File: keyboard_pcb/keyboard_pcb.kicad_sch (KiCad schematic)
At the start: 190 parts, among them SW1 SW_Push, U1 ATmega32U4-A, Y1 16MHz

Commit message: Complete electronic schematic
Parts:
- SW1: renamed from ESC; value MX-NoLED -> ESC
- SW10: renamed from F9; value MX-NoLED -> F9
- SW11: renamed from F10; value MX-NoLED -> F10
- SW12: renamed from F11; value MX-NoLED -> F11
- SW13: renamed from F12; value MX-NoLED -> F12
- SW14: renamed from PRNTSC; value MX-NoLED -> PRNTSC
- SW15: renamed from SCRLLK; value MX-NoLED -> SCRLLK
- SW16: renamed from PBRK; value MX-NoLED -> PBRK
- SW17: renamed from TILDE; value MX-NoLED -> `
- SW18: renamed from N1; value MX-NoLED -> #1
- SW19: renamed from N2; value MX-NoLED -> #2
- SW2: renamed from F1; value MX-NoLED -> F1
- SW20: renamed from N3; value MX-NoLED -> #3
- SW21: renamed from N4; value MX-NoLED -> #4
- SW22: renamed from N5; value MX-NoLED -> #5
- SW23: renamed from N6; value MX-NoLED -> #6
- SW24: renamed from N7; value MX-NoLED -> #7
- SW25: renamed from N8; value MX-NoLED -> #8
- SW26: renamed from N9; value MX-NoLED -> #9
- SW27: renamed from N0; value MX-NoLED -> #0
- SW28: renamed from -; value MX-NoLED -> -
- SW29: renamed from =; value MX-NoLED -> =
- SW3: renamed from F2; value MX-NoLED -> F2
- SW30: renamed from BKSPC; value MX-NoLED -> BKSPC
- SW31: renamed from INS; value MX-NoLED -> INS
- SW32: renamed from HOME; value MX-NoLED -> HOME
- SW33: renamed from PGUP; value MX-NoLED -> PGUP
- SW34: renamed from TAB; value MX-NoLED -> TAB
- SW35: renamed from Q; value MX-NoLED -> Q
- SW36: renamed from W; value MX-NoLED -> W
- SW37: renamed from E; value MX-NoLED -> E
- SW38: renamed from R; value MX-NoLED -> R
- SW39: renamed from T; value MX-NoLED -> T
- SW4: renamed from F3; value MX-NoLED -> F3
- SW40: renamed from Y; value MX-NoLED -> Y
- SW41: renamed from U; value MX-NoLED -> U
- SW42: renamed from I; value MX-NoLED -> I
- SW43: renamed from O; value MX-NoLED -> O
- SW44: renamed from P; value MX-NoLED -> P
- SW45: renamed from [; value MX-NoLED -> [
- SW46: renamed from ]; value MX-NoLED -> ]
- SW47: renamed from \; value MX-NoLED -> \
- SW48: renamed from DEL; value MX-NoLED -> DEL
- SW49: renamed from END; value MX-NoLED -> END
- SW5: renamed from F4; value MX-NoLED -> F4
- SW50: renamed from PGDN; value MX-NoLED -> PGDN
- SW51: renamed from CAPSLK; value MX-NoLED -> CAPSLK
- SW52: renamed from A; value MX-NoLED -> A
- SW53: renamed from S; value MX-NoLED -> S
- SW54: renamed from D; value MX-NoLED -> D
- SW55: renamed from F; value MX-NoLED -> F
- SW56: renamed from G; value MX-NoLED -> G
- SW57: renamed from H; value MX-NoLED -> H
- SW58: renamed from J; value MX-NoLED -> J
- SW59: renamed from K; value MX-NoLED -> K
- SW6: renamed from F5; value MX-NoLED -> F5
- SW60: renamed from L; value MX-NoLED -> L
- SW61: renamed from ;; value MX-NoLED -> ;
- SW62: renamed from '; value MX-NoLED -> '
- SW63: renamed from ENTER; value MX-NoLED -> ENTER
- SW64: renamed from LSHIFT; value MX-NoLED -> LSHIFT
- SW65: renamed from Z; value MX-NoLED -> Z
- SW66: renamed from X; value MX-NoLED -> X
- SW67: renamed from C; value MX-NoLED -> C
- SW68: renamed from V; value MX-NoLED -> V
- SW69: renamed from B; value MX-NoLED -> B
- SW7: renamed from F6; value MX-NoLED -> F6
- SW70: renamed from N; value MX-NoLED -> N
- SW71: renamed from M; value MX-NoLED -> M
- SW72: renamed from ,; value MX-NoLED -> ,
- SW73: renamed from .; value MX-NoLED -> .
- SW74: renamed from /; value MX-NoLED -> /
- SW75: renamed from RSHIFT; value MX-NoLED -> RSHIFT
- SW76: renamed from UP; value MX-NoLED -> UP
- SW77: renamed from LCTRL; value MX-NoLED -> LCTRL
- SW78: renamed from LWIN; value MX-NoLED -> LWIN
- SW79: renamed from LALT; value MX-NoLED -> LALT
- SW8: renamed from F7; value MX-NoLED -> F7
- SW80: renamed from SPACE; value MX-NoLED -> SPACE
- SW81: renamed from RALT; value MX-NoLED -> RALT
- SW82: renamed from RWIN; value MX-NoLED -> RWIN
- SW83: renamed from MENU; value MX-NoLED -> MENU
- SW84: renamed from RCTRL; value MX-NoLED -> RCTRL
- SW85: renamed from LEFT; value MX-NoLED -> LEFT
- SW86: renamed from DOWN; value MX-NoLED -> DOWN
- SW87: renamed from RIGHT; value MX-NoLED -> RIGHT
- SW9: renamed from F8; value MX-NoLED -> F8
- renumbered D86 to D1, D96 to D10, D97 to D11, D98 to D12, D99 to D13, D100 to D14, D101 to D15, D102 to D16, D1 to D17, D6 to D18, D11 to D19, D88 to D2, D16 to D20, D26 to D22, D31 to D23, D36 to D24, D41 to D25, D46 to D26, D51 to D27, D56 to D28, D61 to D29, D89 to D3, D66 to D30, D71 to D31, D76 to D32, D81 to D33, D2 to D34, D7 to D35, D12 to D36, D17 to D37, D22 to D38, D27 to D39, D90 to D4, D32 to D40, D37 to D41, D47 to D43, D52 to D44, D57 to D45, D62 to D46, D67 to D47, D72 to D48, D77 to D49, D91 to D5, D82 to D50, D3 to D51, D8 to D52, D13 to D53, D18 to D54, D23 to D55, D28 to D56, D33 to D57, D38 to D58, D43 to D59, D92 to D6, D48 to D60, D53 to D61, D58 to D62, D68 to D63, D4 to D64, D14 to D65, D19 to D66, D24 to D67, D29 to D68, D34 to D69, D93 to D7, D39 to D70, D44 to D71, D49 to D72, D54 to D73, D59 to D74, D69 to D75, D79 to D76, D5 to D77, D10 to D78, D15 to D79, D94 to D8, D35 to D80, D55 to D81, D60 to D82, D65 to D83, D70 to D84, D75 to D85, D80 to D86, D85 to D87, D95 to D9, SW1 to SW88
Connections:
- net COL0: now also U1.25 (PD4)
- net COL1: now also U1.26 (PD6)
- net COL10: now also U1.9 (PB1)
- net COL11: now also U1.10 (PB2)
- net COL12: now also U1.11 (PB3)
- net COL13: now also U1.18 (PD0)
- net COL14: now also U1.19 (PD1)
- net COL15: now also U1.20 (PD2)
- net COL16: now also U1.21 (PD3)
- net COL2: now also U1.27 (PD7)
- net COL3: now also U1.28 (PB4)
- net COL5: now also U1.29 (PB5)
- net COL6: now also U1.30 (PB6)
- net COL7: now also U1.31 (PC6)
- net COL8: now also U1.32 (PC7)
- net COL9: now also U1.8 (PB0)
- net ROW0: now also U1.36 (PF7)
- net ROW1: now also U1.37 (PF6)
- net ROW2: now also U1.38 (PF5)
- net ROW3: now also U1.39 (PF4)
- net ROW4: now also U1.40 (PF1)
- net ROW5: now also U1.41 (PF0)
- no-connect marks 0 -> 6
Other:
- moved on the sheet: F1

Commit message: PCB layout first draft
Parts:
- C1: value C_Small -> 1uF; footprint (none) -> Capacitor_SMD:C_0805_2012Metric_Pad1.18x1.45mm_HandSolder
- C2, C3, C4, C5, C6, C7: footprint (none) -> Capacitor_SMD:C_0805_2012Metric_Pad1.18x1.45mm_HandSolder
- D1, D10, D11, D12, D13, D14, D15, D16, D17, D18, D19, D2, D20, D21, D22, D23, D24, D25, D26, D27, D28, D29, D3, D30, D31, D32, D33, D34, D35, D36, D37, D38, D39, D4, D40, D41, D42, D43, D44, D45, D46, D47, D48, D49, D5, D50, D51, D52, D53, D54, D55, D56, D57, D58, D59, D6, D60, D61, D62, D63, D64, D65, D66, D67, D68, D69, D7, D70, D71, D72, D73, D74, D75, D76, D77, D78, D79, D8, D80, D81, D82, D83, D84, D85, D86, D87, D9: footprint (none) -> Diode_SMD:D_SOD-123
- F1: footprint (none) -> Fuse:Fuse_1206_3216Metric_Pad1.42x1.75mm_HandSolder
- R1, R2, R3, R4: footprint (none) -> Resistor_SMD:R_0805_2012Metric_Pad1.20x1.40mm_HandSolder
- SW1, SW10, SW11, SW12, SW13, SW14, SW15, SW16, SW17, SW18, SW19, SW2, SW20, SW21, SW22, SW23, SW24, SW25, SW26, SW27, SW28, SW29, SW3, SW31, SW32, SW33, SW35, SW36, SW37, SW38, SW39, SW4, SW40, SW41, SW42, SW43, SW44, SW45, SW46, SW48, SW49, SW5, SW50, SW52, SW53, SW54, SW55, SW56, SW57, SW58, SW59, SW6, SW60, SW61, SW62, SW65, SW66, SW67, SW68, SW69, SW7, SW70, SW71, SW72, SW73, SW74, SW76, SW8, SW85, SW86, SW87, SW9: footprint (none) -> Button_Switch_Keyboard:SW_Cherry_MX_1.00u_PCB
- SW30: footprint (none) -> Button_Switch_Keyboard:SW_Cherry_MX_2.00u_PCB
- SW34, SW47: footprint (none) -> Button_Switch_Keyboard:SW_Cherry_MX_1.50u_PCB
- SW51: footprint (none) -> Button_Switch_Keyboard:SW_Cherry_MX_1.75u_PCB
- SW63, SW64: footprint (none) -> Button_Switch_Keyboard:SW_Cherry_MX_2.25u_PCB
- SW75: footprint (none) -> Button_Switch_Keyboard:SW_Cherry_MX_2.75u_PCB
- SW77, SW78, SW79, SW81, SW82, SW83, SW84: footprint (none) -> Button_Switch_Keyboard:SW_Cherry_MX_1.25u_PCB
- SW80: footprint (none) -> Button_Switch_Keyboard:SW_Cherry_MX_6.25u_PCB
- SW88: footprint (none) -> Button_Switch_SMD:SW_SPST_SKQG_WithStem
- USB1: footprint (none) -> random-keyboard-parts:Molex-0548190589
- Y1: footprint (none) -> Crystal:Crystal_SMD_3225-4Pin_3.2x2.5mm_HandSoldering

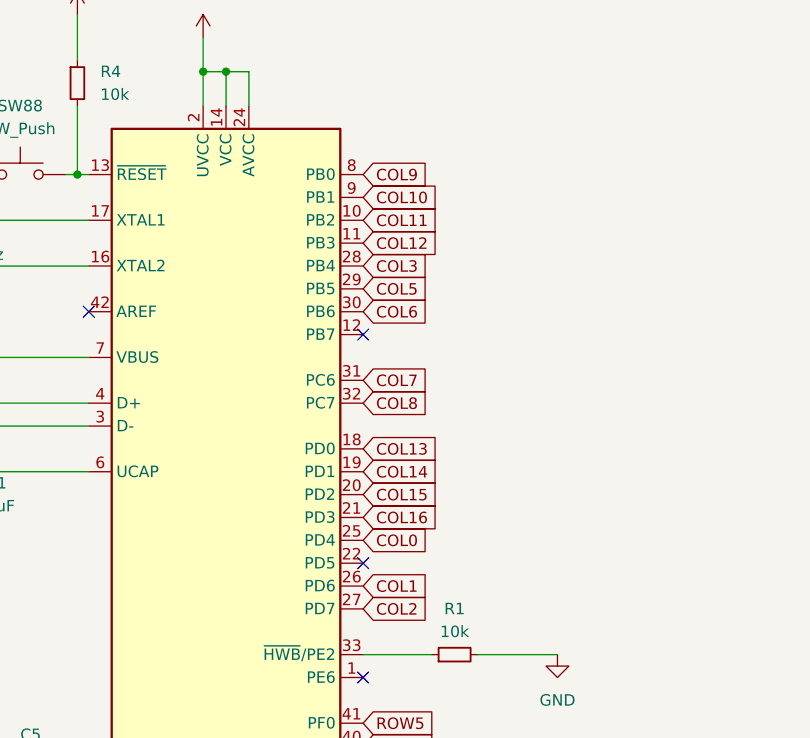
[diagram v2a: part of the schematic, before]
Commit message: Add row/column traces
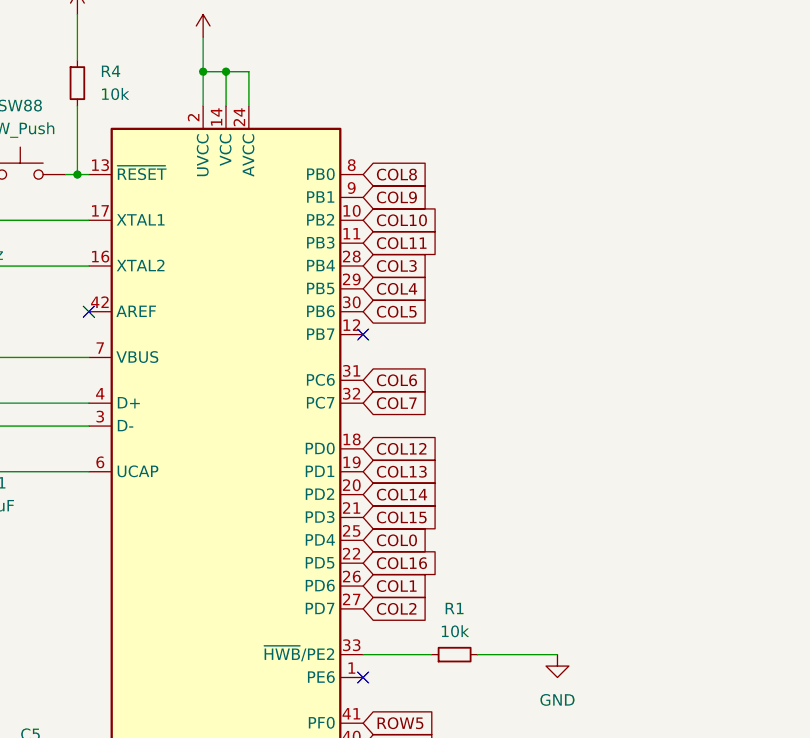
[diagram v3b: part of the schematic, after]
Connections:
- net COL10: now also U1.10 (PB2); no longer U1.9 (PB1)
- net COL11: now also U1.11 (PB3); no longer U1.10 (PB2)
- net COL12: now also U1.18 (PD0); no longer U1.11 (PB3)
- net COL13: now also U1.19 (PD1); no longer U1.18 (PD0)
- net COL14: now also U1.20 (PD2); no longer U1.19 (PD1)
- net COL15: now also U1.21 (PD3); no longer U1.20 (PD2)
- net COL16: now also U1.22 (PD5); no longer U1.21 (PD3)
- net COL4: now also U1.29 (PB5)
- net COL5: now also U1.30 (PB6); no longer U1.29 (PB5)
- net COL6: now also U1.31 (PC6); no longer U1.30 (PB6)
- net COL7: now also U1.32 (PC7); no longer U1.31 (PC6)
- net COL8: now also U1.8 (PB0); no longer U1.32 (PC7)
- net COL9: now also U1.9 (PB1); no longer U1.8 (PB0)
- no-connect marks 6 -> 5
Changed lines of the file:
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@@
 	)
 	(no_connect
-		(at 171.45 219.71)
-	)
-	(no_connect
 		(at 323.85 195.58)
 	)
@@
 	(global_label "COL14"
 		(shape input)
-		(at 171.45 209.55 0)
+		(at 171.45 212.09 0)
 		(fields_autoplaced yes)
 		(effects
@@
 		)
 		(property "Intersheetrefs" "${INTERSHEET_REFS}"
-			(at 180.4828 209.55 0)
+			(at 180.4828 212.09 0)
 			(effects
 				(font
@@
 		)
 	)
+	(global_label "COL4"
+		(shape input)
+		(at 171.45 189.23 0)
+		(fields_autoplaced yes)
+		(effects
+			(font
+				(size 1.27 1.27)
+			)
+			(justify left)
+		)
+		(property "Intersheetrefs" "${INTERSHEET_REFS}"
+			(at 179.2733 189.23 0)
+			(effects
+				(font
+					(size 1.27 1.27)
+				)
+				(justify left)
+				(hide yes)
+			)
+		)
+	)
 	(global_label "COL7"
 		(shape input)
-		(at 171.45 199.39 0)
+		(at 171.45 201.93 0)
 		(fields_autoplaced yes)
 		(effects
@@
 		)
 		(property "Intersheetrefs" "${INTERSHEET_REFS}"
-			(at 179.2733 199.39 0)
+			(at 179.2733 201.93 0)
 			(effects
 				(font
@@
 	(global_label "COL10"
 		(shape input)
-		(at 171.45 179.07 0)
+		(at 171.45 181.61 0)
 		(fields_autoplaced yes)
 		(effects
@@
 		)
 		(property "Intersheetrefs" "${INTERSHEET_REFS}"
-			(at 180.4828 179.07 0)
+			(at 180.4828 181.61 0)
 			(effects
 				(font
@@
 	(global_label "COL8"
 		(shape input)
-		(at 171.45 201.93 0)
+		(at 171.45 176.53 0)
 		(fields_autoplaced yes)
 		(effects
@@
 		)
 		(property "Intersheetrefs" "${INTERSHEET_REFS}"
-			(at 179.2733 201.93 0)
+			(at 179.2733 176.53 0)
 			(effects
 				(font
@@
 	(global_label "COL15"
 		(shape input)
-		(at 171.45 212.09 0)
+		(at 171.45 214.63 0)
 		(fields_autoplaced yes)
 		(effects
@@
 		)
 		(property "Intersheetrefs" "${INTERSHEET_REFS}"
-			(at 180.4828 212.09 0)
+			(at 180.4828 214.63 0)
 			(effects
 				(font
@@
 	(global_label "COL11"
 		(shape input)
-		(at 171.45 181.61 0)
+		(at 171.45 184.15 0)
 		(fields_autoplaced yes)
 		(effects
@@
 		)
 		(property "Intersheetrefs" "${INTERSHEET_REFS}"
-			(at 180.4828 181.61 0)
+			(at 180.4828 184.15 0)
 			(effects
 				(font
@@
 	(global_label "COL9"
 		(shape input)
-		(at 171.45 176.53 0)
+		(at 171.45 179.07 0)
 		(fields_autoplaced yes)
 		(effects
@@
 		)
 		(property "Intersheetrefs" "${INTERSHEET_REFS}"
-			(at 179.2733 176.53 0)
+			(at 179.2733 179.07 0)
 			(effects
 				(font
@@
 	(global_label "COL12"
 		(shape input)
-		(at 171.45 184.15 0)
+		(at 171.45 207.01 0)
 		(fields_autoplaced yes)
 		(effects
@@
 		)
 		(property "Intersheetrefs" "${INTERSHEET_REFS}"
-			(at 180.4828 184.15 0)
+			(at 180.4828 207.01 0)
 			(effects
 				(font
@@
 	(global_label "COL5"
 		(shape input)
-		(at 171.45 189.23 0)
+		(at 171.45 191.77 0)
 		(fields_autoplaced yes)
 		(effects
@@
 		)
 		(property "Intersheetrefs" "${INTERSHEET_REFS}"
-			(at 179.2733 189.23 0)
+			(at 179.2733 191.77 0)
 			(effects
 				(font
@@
 	(global_label "COL13"
 		(shape input)
-		(at 171.45 207.01 0)
+		(at 171.45 209.55 0)
 		(fields_autoplaced yes)
 		(effects
@@
 		)
 		(property "Intersheetrefs" "${INTERSHEET_REFS}"
-			(at 180.4828 207.01 0)
+			(at 180.4828 209.55 0)
 			(effects
 				(font
@@
 	(global_label "COL16"
 		(shape input)
-		(at 171.45 214.63 0)
+		(at 171.45 219.71 0)
 		(fields_autoplaced yes)
 		(effects
@@
 		)
 		(property "Intersheetrefs" "${INTERSHEET_REFS}"
-			(at 180.4828 214.63 0)
+			(at 180.4828 219.71 0)
 			(effects
 				(font
@@
 	(global_label "COL6"
 		(shape input)
-		(at 171.45 191.77 0)
+		(at 171.45 199.39 0)
 		(fields_autoplaced yes)
 		(effects
@@
 		)
 		(property "Intersheetrefs" "${INTERSHEET_REFS}"
-			(at 179.2733 191.77 0)
+			(at 179.2733 199.39 0)
 			(effects
 				(font

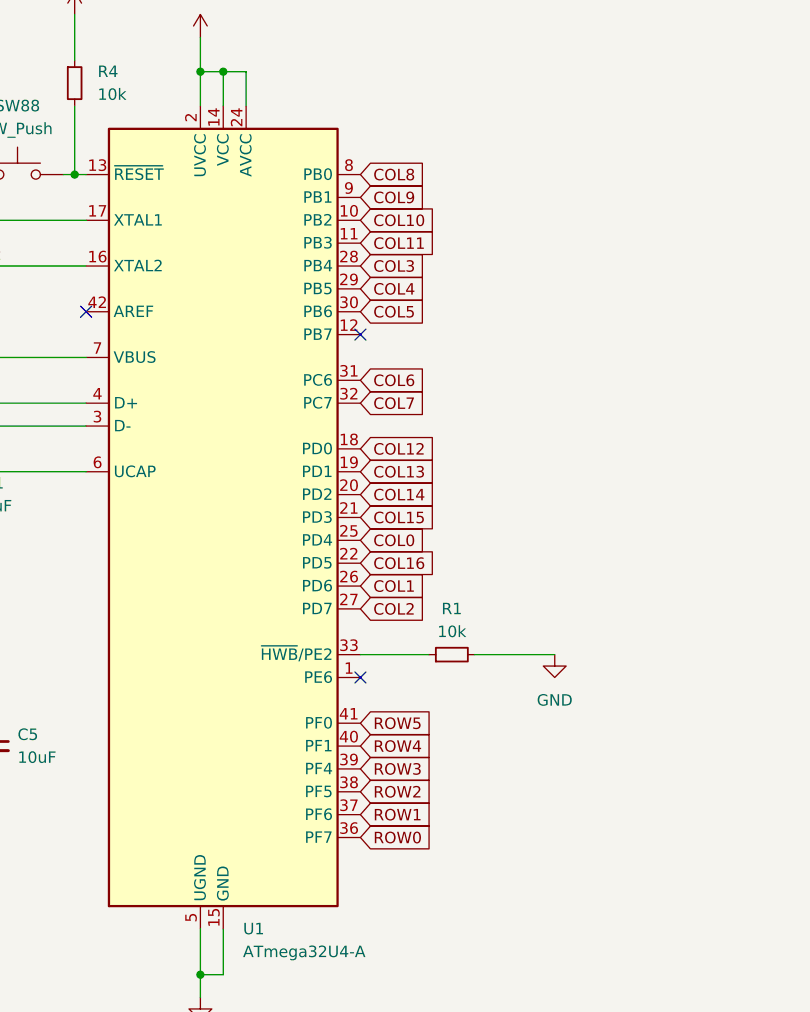
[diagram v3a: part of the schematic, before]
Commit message: PCB complete routing
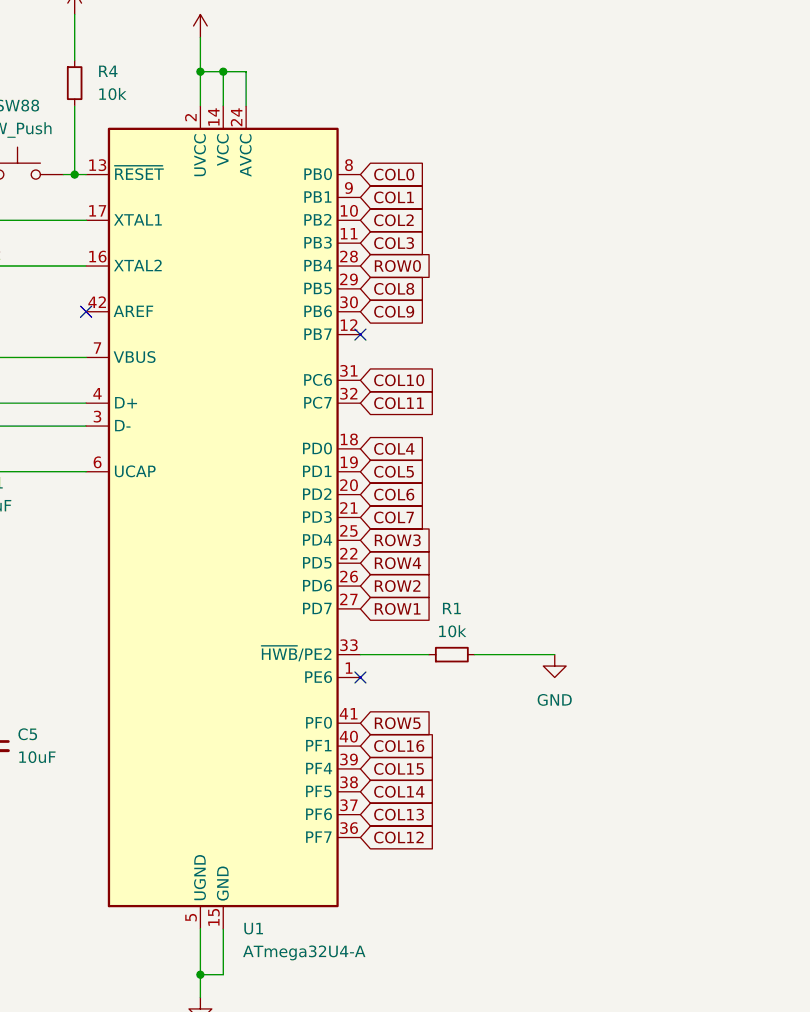
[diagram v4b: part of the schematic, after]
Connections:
- net COL0: now also U1.8 (PB0); no longer U1.25 (PD4)
- net COL1: now also U1.9 (PB1); no longer U1.26 (PD6)
- net COL10: now also U1.31 (PC6); no longer U1.10 (PB2)
- net COL11: now also U1.32 (PC7); no longer U1.11 (PB3)
- net COL12: now also U1.36 (PF7); no longer U1.18 (PD0)
- net COL13: now also U1.37 (PF6); no longer U1.19 (PD1)
- net COL14: now also U1.38 (PF5); no longer U1.20 (PD2)
- net COL15: now also U1.39 (PF4); no longer U1.21 (PD3)
- net COL16: now also U1.40 (PF1); no longer U1.22 (PD5)
- net COL2: now also U1.10 (PB2); no longer U1.27 (PD7)
- net COL3: now also U1.11 (PB3); no longer U1.28 (PB4)
- net COL4: now also U1.18 (PD0); no longer U1.29 (PB5)
- net COL5: now also U1.19 (PD1); no longer U1.30 (PB6)
- net COL6: now also U1.20 (PD2); no longer U1.31 (PC6)
- net COL7: now also U1.21 (PD3); no longer U1.32 (PC7)
- net COL8: now also U1.29 (PB5); no longer U1.8 (PB0)
- net COL9: now also U1.30 (PB6); no longer U1.9 (PB1)
- net ROW0: now also U1.28 (PB4); no longer U1.36 (PF7)
- net ROW1: now also U1.27 (PD7); no longer U1.37 (PF6)
- net ROW2: now also U1.26 (PD6); no longer U1.38 (PF5)
- net ROW3: now also U1.25 (PD4); no longer U1.39 (PF4)
- net ROW4: now also U1.22 (PD5); no longer U1.40 (PF1)
